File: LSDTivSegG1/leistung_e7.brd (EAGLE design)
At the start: 160 x 100 mm, 80 parts, among them IC1 LM 2576 T5,0, IC2 IR2184D, IC3 IR2184D, IC4 4081N, IC5 4069N, IC6 LM 2576 T15, IC7 IR2184D, IC8 IR2184D, IC9 TINY13-20PU, X1 057-010-1, X2 MKDSN1,5/2-5,08

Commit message: eagle 7 export
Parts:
- added C19, C20: 4m7, rcl:E7,5-18
- added R11, R12, R13, R25: 470k, rcl:0207/7
- added U$2: (no value), lsd2016:BOARD
- C1, C11: value 10u -> 4m7; device rcl:E2,5-5 -> rcl:E7,5-18
- C6: device rcl@1:E2,5-4R -> rcl:E5-13
- C9: device rcl@1:E5-13 -> rcl:E5-13
- D1, D13, D14, D2: value 1N4001 -> 1N4002
- D15, D16, D17, D18, D3, D4, D5, D6: value 18 -> ZD-5W_18V
- D7, D8: value 1N 5711 -> 1N5822
- Q1, Q10, Q11, Q12, Q2, Q3, Q4, Q9: value (none) -> IRFB3077
- R10: value (none) -> 20k
- moved C6 542.3 mm to (232.4, 94.0)
- moved C18 538.0 mm to (106.7, 52.1), turned to 90 degrees
- moved R19 529.4 mm to (137.2, 163.8)
- moved C11 527.1 mm to (73.7, 189.2), turned to 270 degrees
- moved R18 523.6 mm to (104.1, 165.1), turned to 180 degrees
- moved R20 520.9 mm to (119.4, 163.8)
- moved C7 518.2 mm to (209.6, 85.1)
- moved D7 518.2 mm to (207.0, 90.2)
- moved IC1 518.2 mm to (208.3, 99.1)
- moved L1 518.2 mm to (199.4, 78.7)
- moved LED1 518.2 mm to (199.4, 73.7)
- moved R14 518.2 mm to (209.6, 78.7)
- moved D18 517.7 mm to (119.4, 170.2)
- moved C17 516.2 mm to (106.7, 34.3), turned to 90 degrees
- moved C15 511.3 mm to (135.9, 148.6), turned to 270 degrees
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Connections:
- removed net BAT_PWM_IN: IC9.5
- removed net DIRL_IN_INV: IC5.2
- removed net DIRR_IN_INV: IC5.4
- removed net MOTOR_L_ACTIVE: IC2.2, IC3.2, IC4.3
- removed net MOTOR_R_ACTIVE: IC4.4, IC7.2, IC8.2
- removed net N$15: IC4.10
- removed net N$16: IC4.11
- removed net N$21: IC4.8
- removed net N$22: IC4.9
- removed net N$23: IC4.12
- removed net N$24: IC4.13
- removed net N$29: D16.C, Q10.G, R18.2, R23.1
- removed net NC2: X1.10
- removed net VB: C12.+, C13.+, C2.+, C3.+, D1.C, D13.C, D14.C, D2.C, IC2.8, IC3.8, IC7.8, IC8.8
- new net IN_L: IC2.1, IC4.4
- new net IN_L_INVD: IC3.1, IC4.11
- new net IN_R: IC4.3, IC7.1
- new net IN_R_INVD: IC4.10, IC8.1
- new net N$13: D16.C, Q10.G, R18.2, R23.2
- new net VB1: C2.+, D1.C, IC2.8
- new net VB2: C3.+, D2.C, IC3.8
- new net VB3: C12.+, D13.C, IC7.8
- new net VB4: C13.+, D14.C, IC8.8
- net +24V: now also X1.10
- net BAT_+: now also C19.+, C20.+
- net BAT_PWM: now also IC9.5
- net DIRL: now also IC4.5, IC5.3; no longer IC2.1, IC5.1
- net DIRL_INV: now also IC4.12, IC5.4; no longer IC3.1
- net DIRR: now also IC4.1, IC5.1; no longer IC5.3, IC7.1
- net DIRR_INV: now also IC4.8, IC5.2; no longer IC8.1
- net ENABLE: now also IC2.2, IC3.2, IC7.2, IC8.2, R11.2, R12.2, R13.2, R25.2; no longer IC4.1, IC4.5
- net GND: now also C19.-, C20.-, D16.A, D17.A, D4.A, D5.A, R11.1, R12.1, R13.1, R22.1, R23.1, R25.1, R6.1, R7.1
- net MOTOR_L_+: no longer D4.A, R7.2
- net MOTOR_L_-: no longer D5.A, R6.2
- net MOTOR_PWM_L: now also IC4.13, IC4.6; no longer IC4.2
- net MOTOR_PWM_R: now also IC4.2, IC4.9; no longer IC4.6
- net MOTOR_R_+: no longer D16.A, R23.2
- net MOTOR_R_-: no longer D17.A, R22.2
- net N$32: now also R22.2; no longer R22.1
- net N$5: now also R7.2; no longer R7.1
- net N$8: now also R6.2; no longer R6.1
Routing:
- net MOTOR_L_+: track 0.00 -> 28.0 mm
- net +15V: track 0.00 -> 23.2 mm
- net VB1: track 0.00 -> 15.5 mm
- net ENABLE: track 0.00 -> 9.42 mm
- net MOTOR_R_-: track 0.00 -> 7.62 mm
- net MOTOR_R_+: track 0.00 -> 7.62 mm
- net MOTOR_L_-: track 0.00 -> 7.62 mm
- net BAT_+: track 0.00 -> 7.62 mm
- net N$10: track 0.00 -> 7.40 mm
- net IN_L: track 0.00 -> 6.88 mm
- net N$5: track 0.00 -> 6.13 mm
- net N$6: track 0.00 -> 5.08 mm
- net GND: track 0.00 -> 2.54 mm
- net N$9: track 0.00 -> 2.54 mm
- added copper zone on layer 1, net BAT_+
- added copper zone on layer 16, net GND

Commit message: updated eagle7 copatible exports of display and leistung boards
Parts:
- removed IC1: LM 2576 T5,0, LM2576:TO-220-5_IN-LINE
- removed IC6: LM 2576 T15, LM2576:TO-220-5_IN-LINE
- added IC10: LM 2576 T15, LM2576:TO220-5_STAGGERED
- added IC11: LM 2576 T5.0, LM2576:TO220-5_STAGGERED
- F1, F2, F3: value (none) -> 1A
- L1, L2: device rcl@1:0204/5 -> rcl@1:0207/10
- moved C20 194.0 mm to (25.4, 29.2), turned to 180 degrees
- moved C19 182.1 mm to (26.7, 10.2)
- moved C11 181.6 mm to (10.2, 19.1), turned to 180 degrees
- moved C9 160.6 mm to (141.6, 39.0)
- moved D8 159.0 mm to (127.0, 45.7)
- moved X2 156.2 mm to (142.2, 85.1), turned to 180 degrees
- moved L2 146.6 mm to (124.5, 41.9)
- moved C4 143.5 mm to (64.8, 34.3), turned to 180 degrees
- moved C8 134.7 mm to (118.1, 33.0), turned to 90 degrees
- moved C5 132.7 mm to (64.8, 11.4), turned to 180 degrees
- moved Q9 131.0 mm to (50.8, 55.9), turned to 270 degrees
- moved F3 129.6 mm to (123.2, 85.1)
- moved R15 128.2 mm to (133.3, 35.6), turned to 270 degrees
- moved Q12 126.7 mm to (50.8, 90.2), turned to 270 degrees
- moved Q10 125.6 mm to (50.8, 67.3), turned to 270 degrees
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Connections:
- net +15V: now also IC10.P$4; no longer IC6.P$4
- net +24V: now also IC10.P$1, IC11.P$1; no longer IC1.P$1, IC6.P$1
- net +5V: now also IC11.P$4; no longer IC1.P$4
- net GND: now also IC10.P$3, IC10.P$5, IC11.P$3, IC11.P$5; no longer IC1.P$3, IC1.P$5, IC6.P$3, IC6.P$5
- net N$1: now also IC11.P$2; no longer IC1.P$2
- net N$4: now also IC10.P$2; no longer IC6.P$2
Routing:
- net +5V: track 0.00 -> 211.0 mm, vias 0 -> 1
- net +15V: track 23.2 -> 209.0 mm, vias 0 -> 2
- net GND: track 2.54 -> 181.2 mm, vias 0 -> 7
- net ENABLE: track 9.42 -> 162.1 mm, vias 0 -> 2
- net MOTOR_L_-: track 7.62 -> 154.7 mm
- net MOTOR_R_-: track 7.62 -> 137.3 mm, vias 0 -> 2
- net +24V: track 0.00 -> 124.0 mm, vias 0 -> 3
- net MOTOR_R_+: track 7.62 -> 130.8 mm, vias 0 -> 3
- net MOTOR_L_+: track 28.0 -> 123.8 mm, vias 0 -> 1
- net MOTOR_PWM_L: track 0.00 -> 94.4 mm, vias 0 -> 2
- net MOTOR_PWM_R: track 0.00 -> 94.0 mm, vias 0 -> 2
- net DIRR: track 0.00 -> 84.1 mm, vias 0 -> 4
- net DIRL: track 0.00 -> 79.0 mm, vias 0 -> 2
- net BAT_+: track 7.62 -> 85.1 mm
- net IN_L_INVD: track 0.00 -> 68.1 mm, vias 0 -> 2
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- added copper zone on layer 16, net BAT_+
- removed copper zone on layer 1, net BAT_+
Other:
- board size 160 x 100 mm -> 150 x 100 mm
- board text added: "LSD-GR1-LST-D-T"
- board text added: "LSD-GR1-REG-D-+"
- board text added: "LSD-GR1-REG-D-BSTOP"
- board text added: "LSD-GR1-REG-D-TStop"

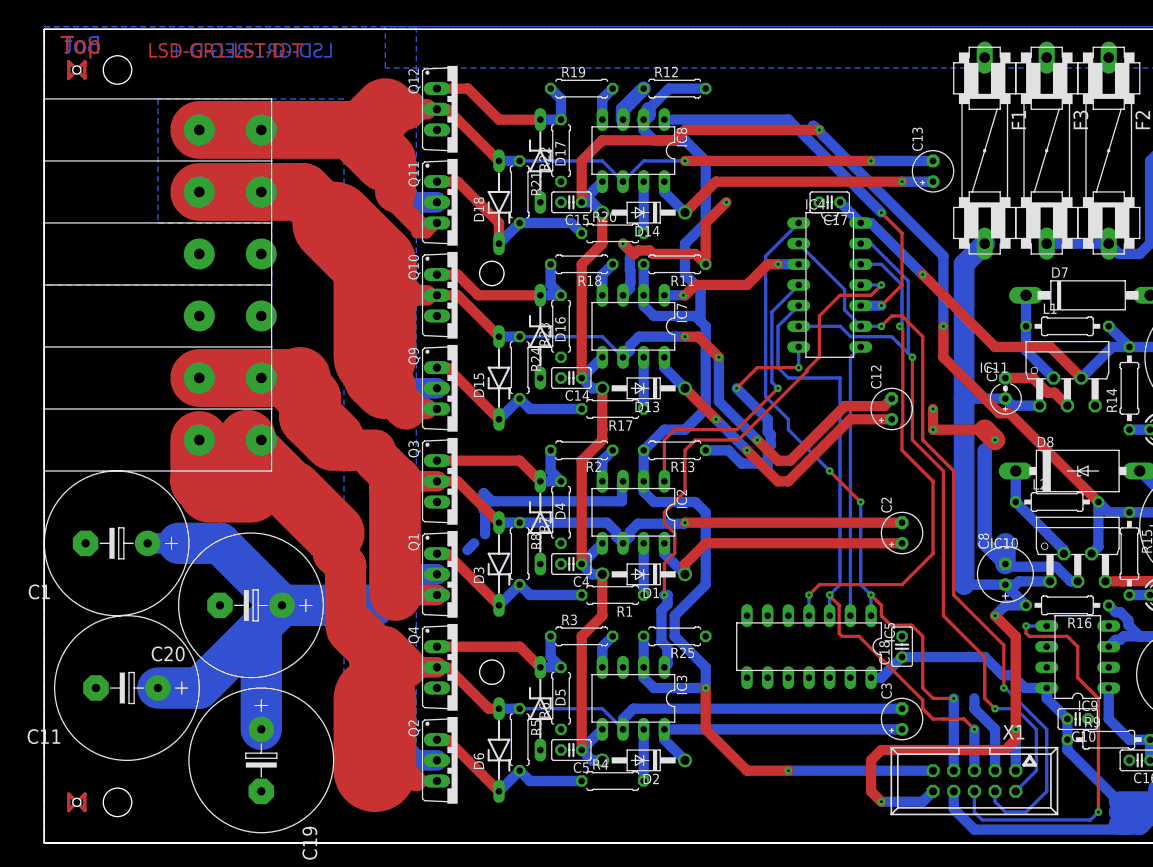
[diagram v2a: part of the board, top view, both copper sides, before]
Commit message: fixes aus der Nachbesprechung
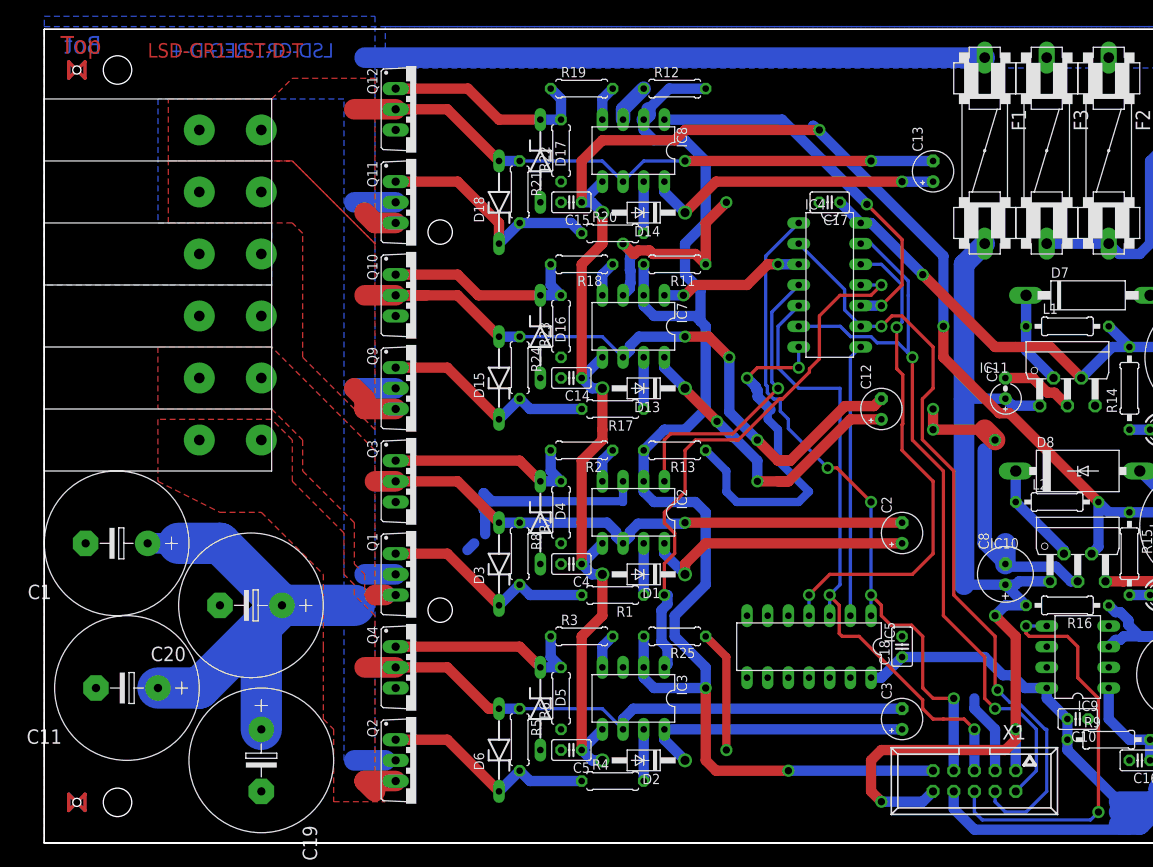
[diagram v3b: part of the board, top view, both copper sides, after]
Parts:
- moved Q1 5.08 mm to (45.7, 33.0)
- moved Q10 5.08 mm to (45.7, 67.3)
- moved Q11 5.08 mm to (45.7, 78.7)
- moved Q12 5.08 mm to (45.7, 90.2)
- moved Q2 5.08 mm to (45.7, 10.2)
- moved Q3 5.08 mm to (45.7, 44.5)
- moved Q4 5.08 mm to (45.7, 21.6)
- moved Q9 5.08 mm to (45.7, 55.9)
- moved C12 1.27 mm to (102.9, 53.3)
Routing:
- net MOTOR_L_-: track 154.7 -> 76.6 mm
- net BAT_+: track 85.1 -> 159.5 mm
- net MOTOR_R_-: track 137.3 -> 84.0 mm
- net MOTOR_L_+: track 123.8 -> 72.2 mm
- net MOTOR_R_+: track 130.8 -> 94.9 mm
- net GND: track 181.2 -> 208.7 mm, vias 7 -> 8
- net N$8: track 20.6 -> 25.7 mm
- net N$7: track 22.0 -> 27.1 mm
- net N$6: track 22.0 -> 27.1 mm
- net N$5: track 20.6 -> 25.7 mm
- net N$32: track 21.2 -> 26.2 mm
- net N$31: track 24.0 -> 29.1 mm
- net N$30: track 22.0 -> 27.1 mm
- net N$13: track 20.6 -> 25.7 mm
- net ENABLE: track 162.1 -> 164.3 mm
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- added copper zone on layer 1, net MOTOR_L_+
- added copper zone on layer 1, net MOTOR_L_-
- added copper zone on layer 1, net MOTOR_R_+
- added copper zone on layer 1, net MOTOR_R_-
